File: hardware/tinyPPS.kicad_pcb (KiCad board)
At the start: 2 copper layers, 63 x 37 mm, 68 parts, among them IC1 AP2205-33Y-13, IC2 AP33772SDKZ-13-FA01, J1 USB_C_Receptacle_USB2.0_14P, J2 187-3802, J3 187-3802, J5 SM03B-SRSS-TB_LF__SN_, Q1 DMN3009SFG-7, Q2 DMN3009SFG-7, Q3 BSS123, Q4 BSS123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

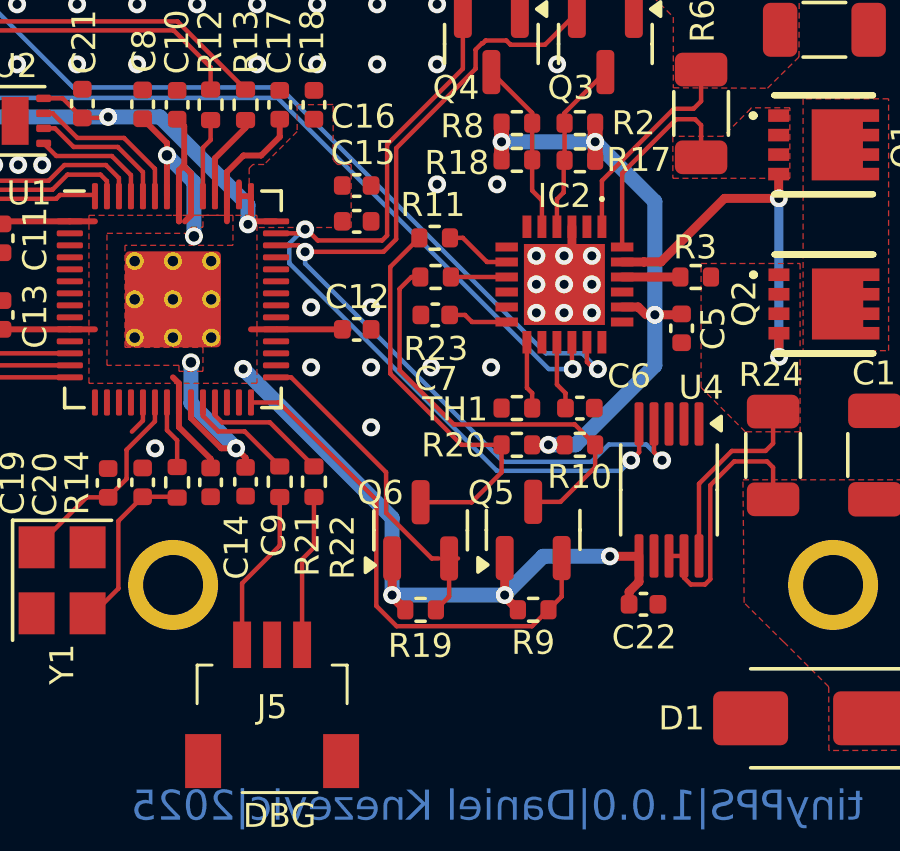
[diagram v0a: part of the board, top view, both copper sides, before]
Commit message: Remove LED connection and update PD_INT level shifter
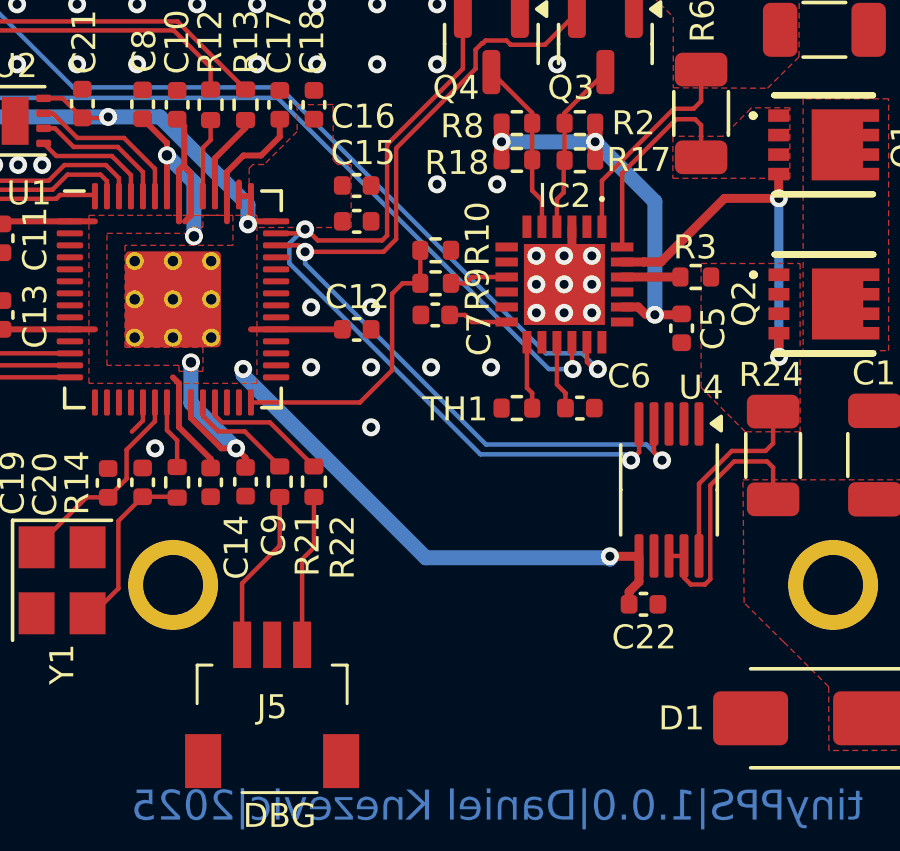
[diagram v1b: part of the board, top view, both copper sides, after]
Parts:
- removed Q5, Q6: BSS123, Package_TO_SOT_SMD:SOT-23
- removed R11, R23: 0R, Resistor_SMD:R_0402_1005Metric
- removed R19, R20: 10k, Resistor_SMD:R_0402_1005Metric
- R24: value TODO -> 10m
- R9: value 10k -> 5k1
- moved R9 11.4 mm to (109.5, 91.3), turned to 180 degrees
- moved R10 8.07 mm to (109.5, 90.2)
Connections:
- IC2 pad 8: Net-(IC2-LED) -> unconnected-(IC2-LED-Pad8)
- IC2 pad 9: Net-(IC2-INT) -> /PD_INT_5V
- R10 pad 1: +5V -> /PD_INT
- R10 pad 2: /PD_INT_5V -> GND
- R9 pad 1: +3V3 -> /PD_INT_5V
- U1 pad 29: /PD_LED -> unconnected-(U1-GPIO18-Pad29)
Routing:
- net /PD_LED_5V: track 13.4 -> 0.00 mm
- net /PD_INT_5V: track 14.1 -> 1.95 mm
- net /PD_LED: track 11.0 -> 0.00 mm
- net +5V: track 21.4 -> 14.0 mm, vias 4 -> 3
- net /PD_INT: track 17.2 -> 9.88 mm
- net +3V3: track 107.1 -> 101.1 mm, vias 10 -> 8
- net Net-(IC2-LED): track 2.22 -> 0.00 mm
- net Net-(IC2-INT): track 1.86 -> 0.00 mm

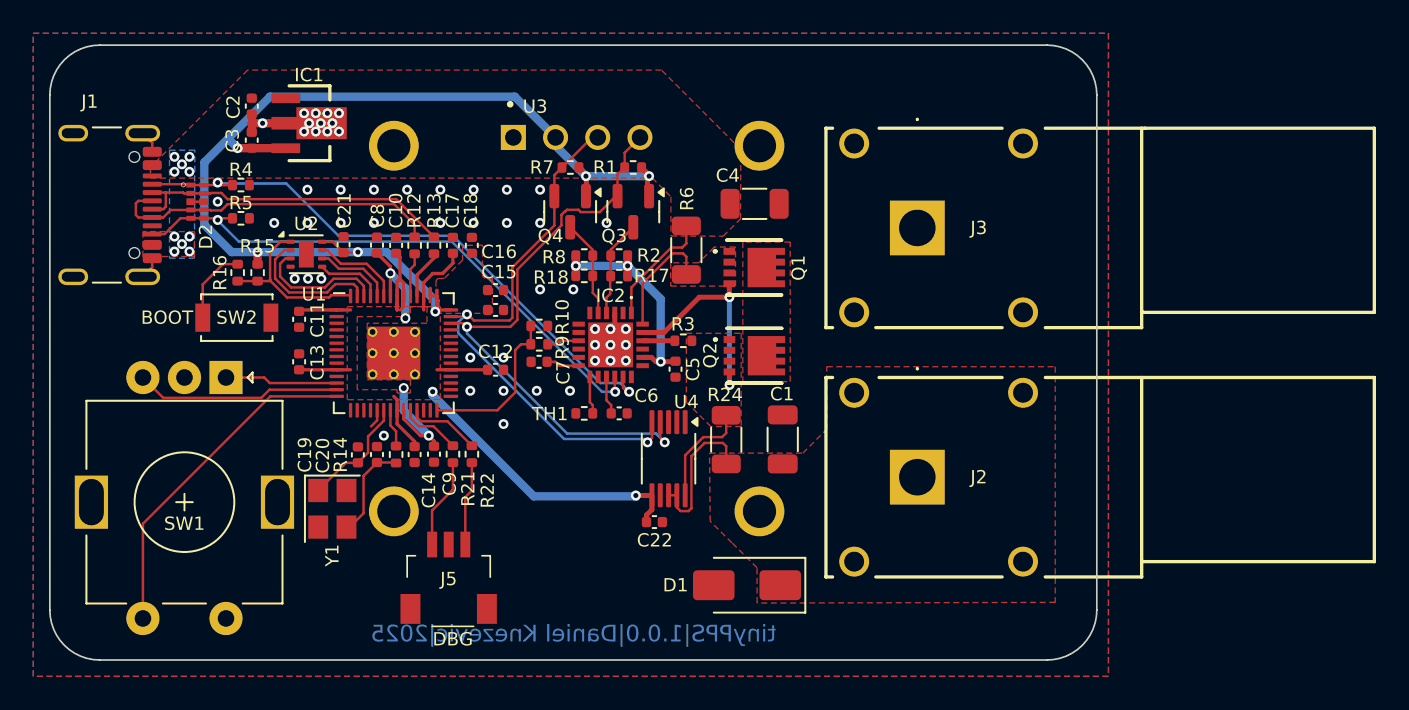
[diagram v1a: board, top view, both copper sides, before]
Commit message: Use back-to-back N MOS switch with common source
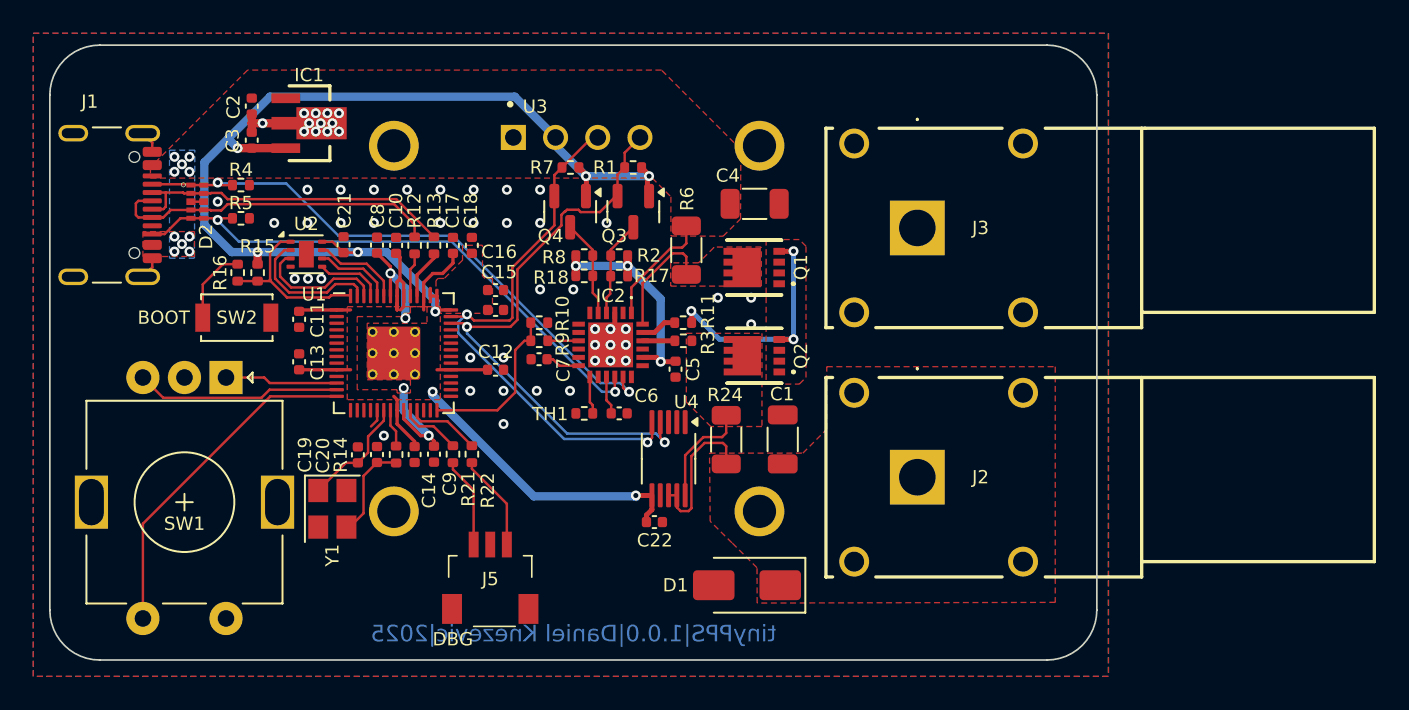
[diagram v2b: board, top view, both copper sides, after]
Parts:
- added R11: 10R, Resistor_SMD:R_0402_1005Metric, F.Cu at (118.2, 90.0)
- moved Q1 2.62 mm to (121.2, 86.7), turned to 90 degrees
- moved Q2 2.62 mm to (121.2, 92.0), turned to 90 degrees
- moved J5 2.50 mm to (106.6, 105.8)
- moved R9 0.21 mm to (109.5, 91.1)
- moved R10 0.20 mm to (109.5, 90.0)
- moved C7 0.15 mm to (109.5, 92.2)
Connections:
- Q1 pad 1: Net-(IC2-VCC) -> Net-(Q1-S_1)
- Q1 pad 2: Net-(IC2-VCC) -> Net-(Q1-S_1)
- Q1 pad 3: Net-(IC2-VCC) -> Net-(Q1-S_1)
- Q1 pad 4: Net-(IC2-PWR_EN) -> Net-(Q1-G)
- Q1 pad 5: Net-(Q1-D_1) -> Net-(IC2-VCC)
- Q1 pad 6: Net-(Q1-D_1) -> Net-(IC2-VCC)
- Q1 pad 7: Net-(Q1-D_1) -> Net-(IC2-VCC)
- Q1 pad 8: Net-(Q1-D_1) -> Net-(IC2-VCC)
- Q1 pad 9: Net-(Q1-D_1) -> Net-(IC2-VCC)
- Q2 pad 1: /VIN+ -> Net-(Q1-S_1)
- Q2 pad 2: /VIN+ -> Net-(Q1-S_1)
- Q2 pad 3: /VIN+ -> Net-(Q1-S_1)
- Q2 pad 4: Net-(IC2-PWR_EN) -> Net-(Q1-G)
- Q2 pad 5: Net-(Q1-D_1) -> /VIN+
- Q2 pad 6: Net-(Q1-D_1) -> /VIN+
- Q2 pad 7: Net-(Q1-D_1) -> /VIN+
- Q2 pad 8: Net-(Q1-D_1) -> /VIN+
- Q2 pad 9: Net-(Q1-D_1) -> /VIN+
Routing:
- net Net-(Q1-G): track 0.00 -> 14.6 mm, vias 0 -> 3
- net Net-(IC2-PWR_EN): track 13.0 -> 2.18 mm, vias 2 -> 0
- net GND: vias 52 -> 55
- added copper zone on F.Cu, net Net-(Q1-S_1)
- removed copper zone on F.Cu, net Net-(Q1-D_1)
